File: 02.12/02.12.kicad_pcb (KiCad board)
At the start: 2 copper layers, 220 parts

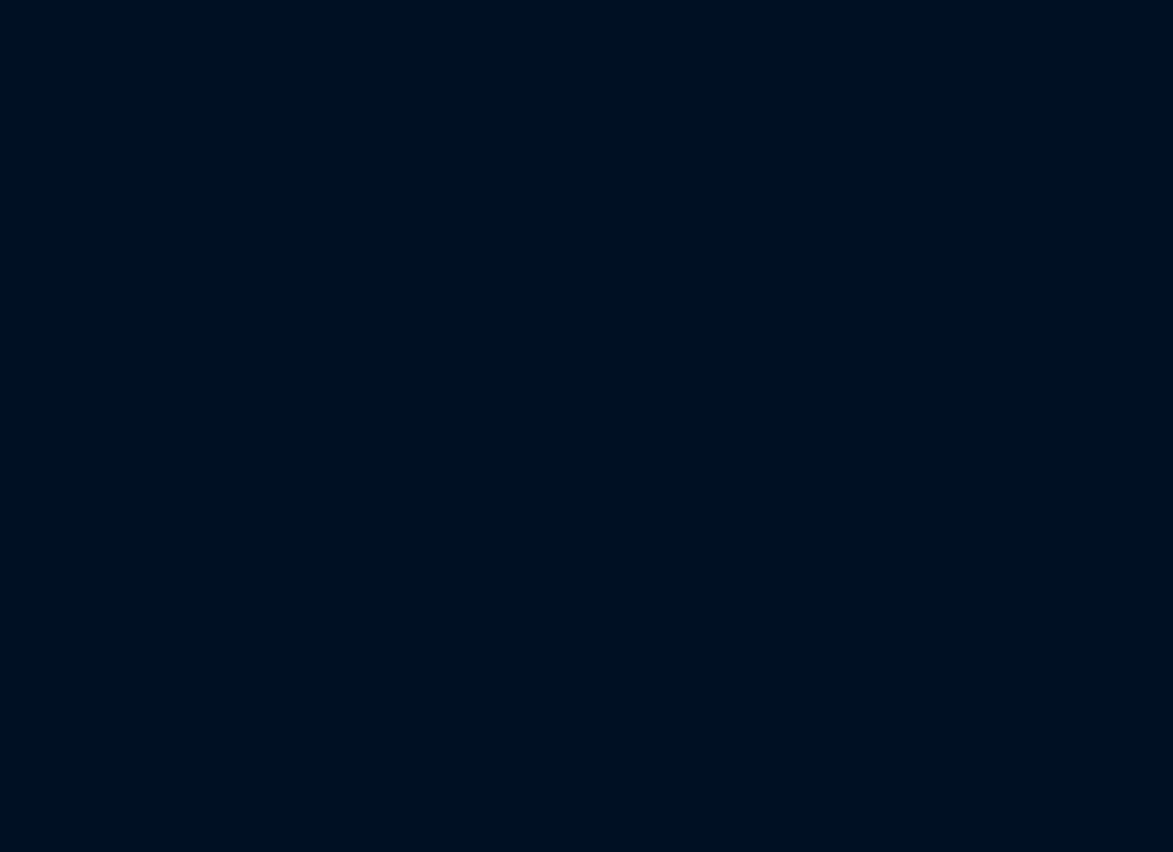
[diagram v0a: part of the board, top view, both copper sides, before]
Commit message: add try folder
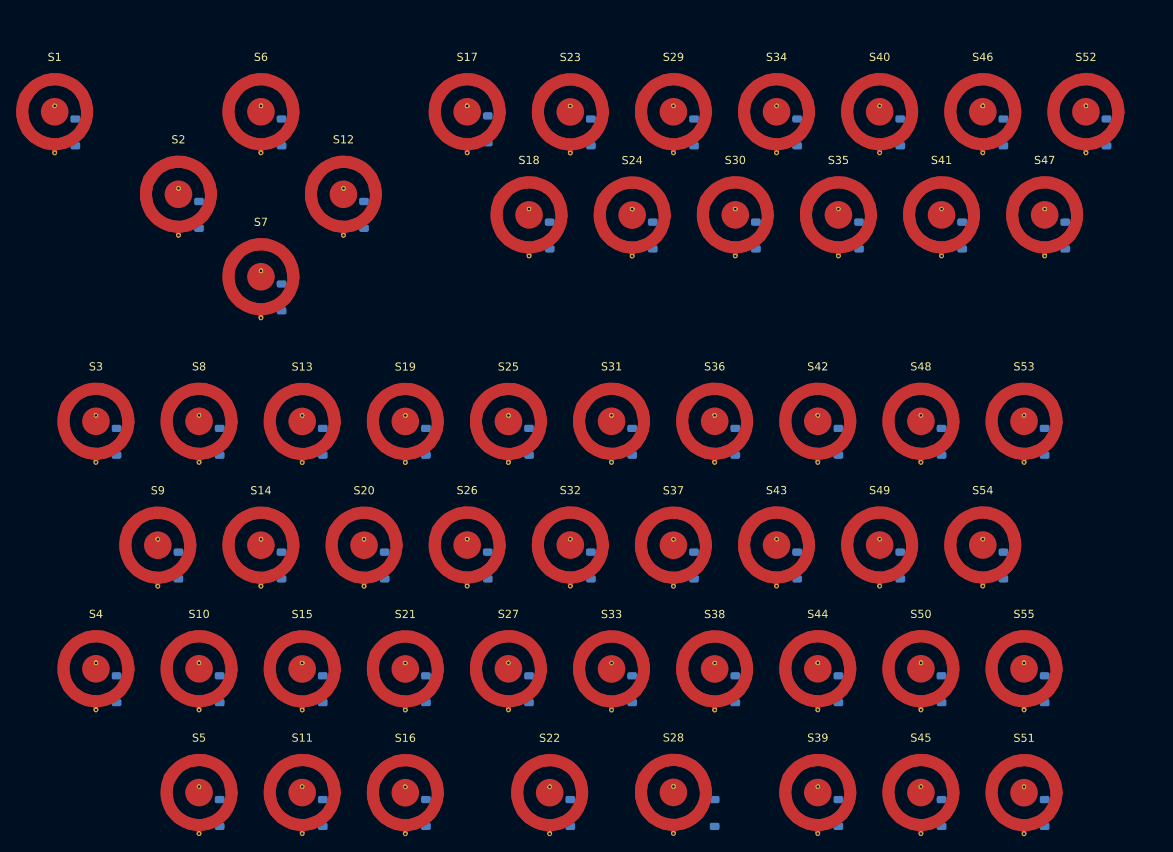
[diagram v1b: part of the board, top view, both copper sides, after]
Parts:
- added D1: Diode, Diode_SMD:D_SOD-123, B.Cu at (-153.2, 151.7)
- added D10: Diode, Diode_SMD:D_SOD-123, B.Cu at (-135.5, 220.3)
- added D11: Diode, Diode_SMD:D_SOD-123, B.Cu at (-122.8, 235.5)
- added D12: Diode, Diode_SMD:D_SOD-123, B.Cu at (-117.7, 161.9)
- added D13: Diode, Diode_SMD:D_SOD-123, B.Cu at (-122.8, 189.8)
- added D14: Diode, Diode_SMD:D_SOD-123, B.Cu at (-127.8, 205.0)
- added D15: Diode, Diode_SMD:D_SOD-123, B.Cu at (-122.8, 220.3)
- added D16: Diode, Diode_SMD:D_SOD-123, B.Cu at (-110.1, 235.5)
- added D17: Diode, Diode_SMD:D_SOD-123, B.Cu at (-102.4, 151.3)
- added D18: Diode, Diode_SMD:D_SOD-123, B.Cu at (-94.8, 164.4)
- added D19: Diode, Diode_SMD:D_SOD-123, B.Cu at (-110.1, 189.8)
- added D2: Diode, Diode_SMD:D_SOD-123, B.Cu at (-138.0, 161.9)
- added D20: Diode, Diode_SMD:D_SOD-123, B.Cu at (-115.1, 205.0)
- added D21: Diode, Diode_SMD:D_SOD-123, B.Cu at (-110.1, 220.3)
- added D22: Diode, Diode_SMD:D_SOD-123, B.Cu at (-92.3, 235.5)
- added D23: Diode, Diode_SMD:D_SOD-123, B.Cu at (-89.7, 151.7)
- added D24: Diode, Diode_SMD:D_SOD-123, B.Cu at (-82.1, 164.4)
- added D25: Diode, Diode_SMD:D_SOD-123, B.Cu at (-97.4, 189.8)
- added D26: Diode, Diode_SMD:D_SOD-123, B.Cu at (-102.4, 205.0)
- added D27: Diode, Diode_SMD:D_SOD-123, B.Cu at (-97.4, 220.3)
- added D28: Diode, Diode_SMD:D_SOD-123, B.Cu at (-74.5, 235.5)
- added D29: Diode, Diode_SMD:D_SOD-123, B.Cu at (-77.0, 151.7)
- added D3: Diode, Diode_SMD:D_SOD-123, B.Cu at (-148.2, 189.8)
- added D30: Diode, Diode_SMD:D_SOD-123, B.Cu at (-69.4, 164.4)
- added D31: Diode, Diode_SMD:D_SOD-123, B.Cu at (-84.7, 189.8)
- added D32: Diode, Diode_SMD:D_SOD-123, B.Cu at (-89.7, 205.0)
- added D33: Diode, Diode_SMD:D_SOD-123, B.Cu at (-84.7, 220.3)
- added D34: Diode, Diode_SMD:D_SOD-123, B.Cu at (-64.3, 151.7)
- added D35: Diode, Diode_SMD:D_SOD-123, B.Cu at (-56.7, 164.4)
- added D36: Diode, Diode_SMD:D_SOD-123, B.Cu at (-72.0, 189.8)
- added D37: Diode, Diode_SMD:D_SOD-123, B.Cu at (-77.0, 205.0)
- added D38: Diode, Diode_SMD:D_SOD-123, B.Cu at (-72.0, 220.3)
- added D39: Diode, Diode_SMD:D_SOD-123, B.Cu at (-59.3, 235.5)
- added D4: Diode, Diode_SMD:D_SOD-123, B.Cu at (-148.2, 220.3)
- added D40: Diode, Diode_SMD:D_SOD-123, B.Cu at (-51.6, 151.7)
- added D41: Diode, Diode_SMD:D_SOD-123, B.Cu at (-44.0, 164.4)
- added D42: Diode, Diode_SMD:D_SOD-123, B.Cu at (-59.3, 189.8)
- added D43: Diode, Diode_SMD:D_SOD-123, B.Cu at (-64.3, 205.0)
- added D44: Diode, Diode_SMD:D_SOD-123, B.Cu at (-59.3, 220.3)
- added D45: Diode, Diode_SMD:D_SOD-123, B.Cu at (-46.6, 235.5)
- added D46: Diode, Diode_SMD:D_SOD-123, B.Cu at (-38.9, 151.7)
- added D47: Diode, Diode_SMD:D_SOD-123, B.Cu at (-31.3, 164.4)
- added D48: Diode, Diode_SMD:D_SOD-123, B.Cu at (-46.6, 189.8)
- added D49: Diode, Diode_SMD:D_SOD-123, B.Cu at (-51.6, 205.0)
- added D5: Diode, Diode_SMD:D_SOD-123, B.Cu at (-135.5, 235.5)
- added D50: Diode, Diode_SMD:D_SOD-123, B.Cu at (-46.6, 220.3)
- added D51: Diode, Diode_SMD:D_SOD-123, B.Cu at (-33.9, 235.5)
- added D52: Diode, Diode_SMD:D_SOD-123, B.Cu at (-26.2, 151.7)
- added D53: Diode, Diode_SMD:D_SOD-123, B.Cu at (-33.9, 189.8)
- added D54: Diode, Diode_SMD:D_SOD-123, B.Cu at (-38.9, 205.0)
- added D55: Diode, Diode_SMD:D_SOD-123, B.Cu at (-33.9, 220.3)
- added D6: Diode, Diode_SMD:D_SOD-123, B.Cu at (-127.8, 151.7)
- added D7: Diode, Diode_SMD:D_SOD-123, B.Cu at (-127.8, 172.0)
- added D8: Diode, Diode_SMD:D_SOD-123, B.Cu at (-135.5, 189.8)
- added D9: Diode, Diode_SMD:D_SOD-123, B.Cu at (-140.5, 205.0)
- added S1: Keyswitch, DomeSwitches:DomeSwitch_8mm_double_sided, F.Cu at (-155.8, 149.2)
- added S10: Keyswitch, DomeSwitches:DomeSwitch_8mm_double_sided, F.Cu at (-138.0, 217.8)
- added S11: Keyswitch, DomeSwitches:DomeSwitch_8mm_double_sided, F.Cu at (-125.3, 233.0)
- added S12: Keyswitch, DomeSwitches:DomeSwitch_8mm_double_sided, F.Cu at (-120.2, 159.3)
- added S13: Keyswitch, DomeSwitches:DomeSwitch_8mm_double_sided, F.Cu at (-125.3, 187.3)
- added S14: Keyswitch, DomeSwitches:DomeSwitch_8mm_double_sided, F.Cu at (-130.4, 202.5)
- added S15: Keyswitch, DomeSwitches:DomeSwitch_8mm_double_sided, F.Cu at (-125.3, 217.8)
- added S16: Keyswitch, DomeSwitches:DomeSwitch_8mm_double_sided, F.Cu at (-112.6, 233.0)
- added S17: Keyswitch, DomeSwitches:DomeSwitch_8mm_double_sided, F.Cu at (-105.0, 149.2)
- added S18: Keyswitch, DomeSwitches:DomeSwitch_8mm_double_sided, F.Cu at (-97.4, 161.9)
- added S19: Keyswitch, DomeSwitches:DomeSwitch_8mm_double_sided, F.Cu at (-112.6, 187.3)
- added S2: Keyswitch, DomeSwitches:DomeSwitch_8mm_double_sided, F.Cu at (-140.5, 159.3)
- added S20: Keyswitch, DomeSwitches:DomeSwitch_8mm_double_sided, F.Cu at (-117.7, 202.5)
- added S21: Keyswitch, DomeSwitches:DomeSwitch_8mm_double_sided, F.Cu at (-112.6, 217.8)
- added S22: Keyswitch, DomeSwitches:DomeSwitch_8mm_double_sided, F.Cu at (-94.8, 233.0)
- added S23: Keyswitch, DomeSwitches:DomeSwitch_8mm_double_sided, F.Cu at (-92.3, 149.2)
- added S24: Keyswitch, DomeSwitches:DomeSwitch_8mm_double_sided, F.Cu at (-84.7, 161.9)
- added S25: Keyswitch, DomeSwitches:DomeSwitch_8mm_double_sided, F.Cu at (-99.9, 187.3)
- added S26: Keyswitch, DomeSwitches:DomeSwitch_8mm_double_sided, F.Cu at (-105.0, 202.5)
- added S27: Keyswitch, DomeSwitches:DomeSwitch_8mm_double_sided, F.Cu at (-99.9, 217.8)
- added S28: Keyswitch, DomeSwitches:DomeSwitch_8mm_double_sided, F.Cu at (-79.6, 233.0)
- added S29: Keyswitch, DomeSwitches:DomeSwitch_8mm_double_sided, F.Cu at (-79.6, 149.2)
- added S3: Keyswitch, DomeSwitches:DomeSwitch_8mm_double_sided, F.Cu at (-150.7, 187.3)
- added S30: Keyswitch, DomeSwitches:DomeSwitch_8mm_double_sided, F.Cu at (-72.0, 161.9)
- added S31: Keyswitch, DomeSwitches:DomeSwitch_8mm_double_sided, F.Cu at (-87.2, 187.3)
- added S32: Keyswitch, DomeSwitches:DomeSwitch_8mm_double_sided, F.Cu at (-92.3, 202.5)
- added S33: Keyswitch, DomeSwitches:DomeSwitch_8mm_double_sided, F.Cu at (-87.2, 217.8)
- added S34: Keyswitch, DomeSwitches:DomeSwitch_8mm_double_sided, F.Cu at (-66.9, 149.2)
- added S35: Keyswitch, DomeSwitches:DomeSwitch_8mm_double_sided, F.Cu at (-59.3, 161.9)
- added S36: Keyswitch, DomeSwitches:DomeSwitch_8mm_double_sided, F.Cu at (-74.5, 187.3)
- added S37: Keyswitch, DomeSwitches:DomeSwitch_8mm_double_sided, F.Cu at (-79.6, 202.5)
- added S38: Keyswitch, DomeSwitches:DomeSwitch_8mm_double_sided, F.Cu at (-74.5, 217.8)
- added S39: Keyswitch, DomeSwitches:DomeSwitch_8mm_double_sided, F.Cu at (-61.8, 233.0)
- added S4: Keyswitch, DomeSwitches:DomeSwitch_8mm_double_sided, F.Cu at (-150.7, 217.8)
- added S40: Keyswitch, DomeSwitches:DomeSwitch_8mm_double_sided, F.Cu at (-54.2, 149.2)
- added S41: Keyswitch, DomeSwitches:DomeSwitch_8mm_double_sided, F.Cu at (-46.6, 161.9)
- added S42: Keyswitch, DomeSwitches:DomeSwitch_8mm_double_sided, F.Cu at (-61.8, 187.3)
- added S43: Keyswitch, DomeSwitches:DomeSwitch_8mm_double_sided, F.Cu at (-66.9, 202.5)
- added S44: Keyswitch, DomeSwitches:DomeSwitch_8mm_double_sided, F.Cu at (-61.8, 217.8)
- added S45: Keyswitch, DomeSwitches:DomeSwitch_8mm_double_sided, F.Cu at (-49.1, 233.0)
- added S46: Keyswitch, DomeSwitches:DomeSwitch_8mm_double_sided, F.Cu at (-41.5, 149.2)
- added S47: Keyswitch, DomeSwitches:DomeSwitch_8mm_double_sided, F.Cu at (-33.9, 161.9)
- added S48: Keyswitch, DomeSwitches:DomeSwitch_8mm_double_sided, F.Cu at (-49.1, 187.3)
- added S49: Keyswitch, DomeSwitches:DomeSwitch_8mm_double_sided, F.Cu at (-54.2, 202.5)
- added S5: Keyswitch, DomeSwitches:DomeSwitch_8mm_double_sided, F.Cu at (-138.0, 233.0)
- added S50: Keyswitch, DomeSwitches:DomeSwitch_8mm_double_sided, F.Cu at (-49.1, 217.8)
- added S51: Keyswitch, DomeSwitches:DomeSwitch_8mm_double_sided, F.Cu at (-36.4, 233.0)
- added S52: Keyswitch, DomeSwitches:DomeSwitch_8mm_double_sided, F.Cu at (-28.8, 149.2)
- added S53: Keyswitch, DomeSwitches:DomeSwitch_8mm_double_sided, F.Cu at (-36.4, 187.3)
- added S54: Keyswitch, DomeSwitches:DomeSwitch_8mm_double_sided, F.Cu at (-41.5, 202.5)
- added S55: Keyswitch, DomeSwitches:DomeSwitch_8mm_double_sided, F.Cu at (-36.4, 217.8)
- added S6: Keyswitch, DomeSwitches:DomeSwitch_8mm_double_sided, F.Cu at (-130.4, 149.2)
- added S7: Keyswitch, DomeSwitches:DomeSwitch_8mm_double_sided, F.Cu at (-130.4, 169.5)
- added S8: Keyswitch, DomeSwitches:DomeSwitch_8mm_double_sided, F.Cu at (-138.0, 187.3)
- added S9: Keyswitch, DomeSwitches:DomeSwitch_8mm_double_sided, F.Cu at (-143.1, 202.5)
